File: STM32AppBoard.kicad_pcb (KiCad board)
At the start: 2 copper layers, 85 x 53 mm, 23 parts, among them SW1 SW_Wuerth_450301014042, U1 DM-OLED096-636, U3 NUCLEO-L412KB, U4 JDY-08-jdy-08

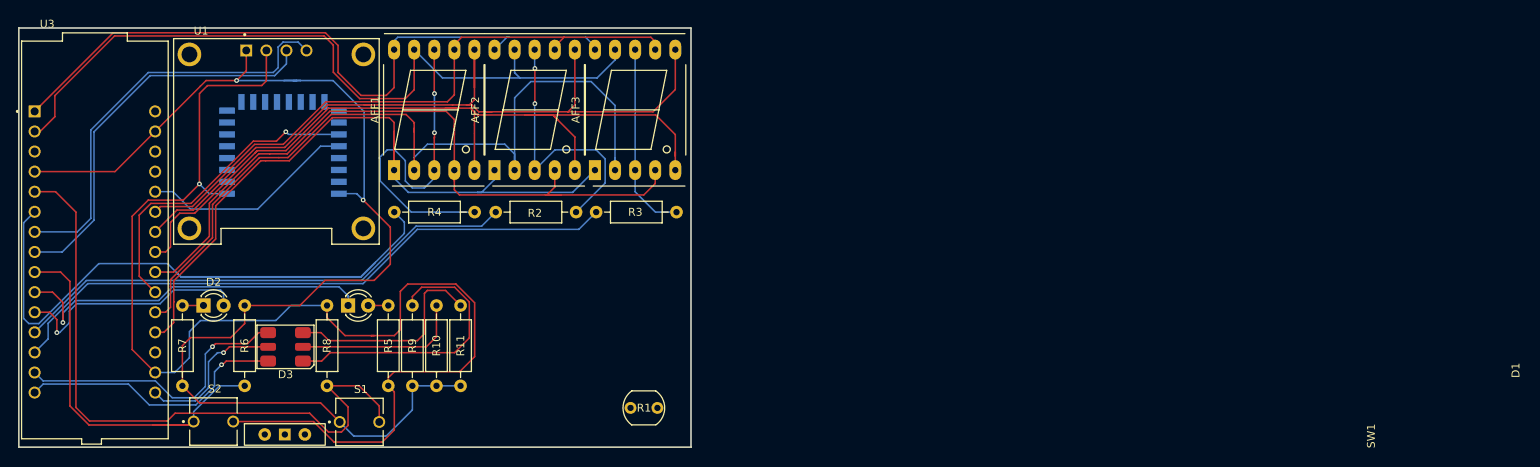
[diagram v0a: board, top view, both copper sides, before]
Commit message: Update STM32AppBoard schematic and PCB layout
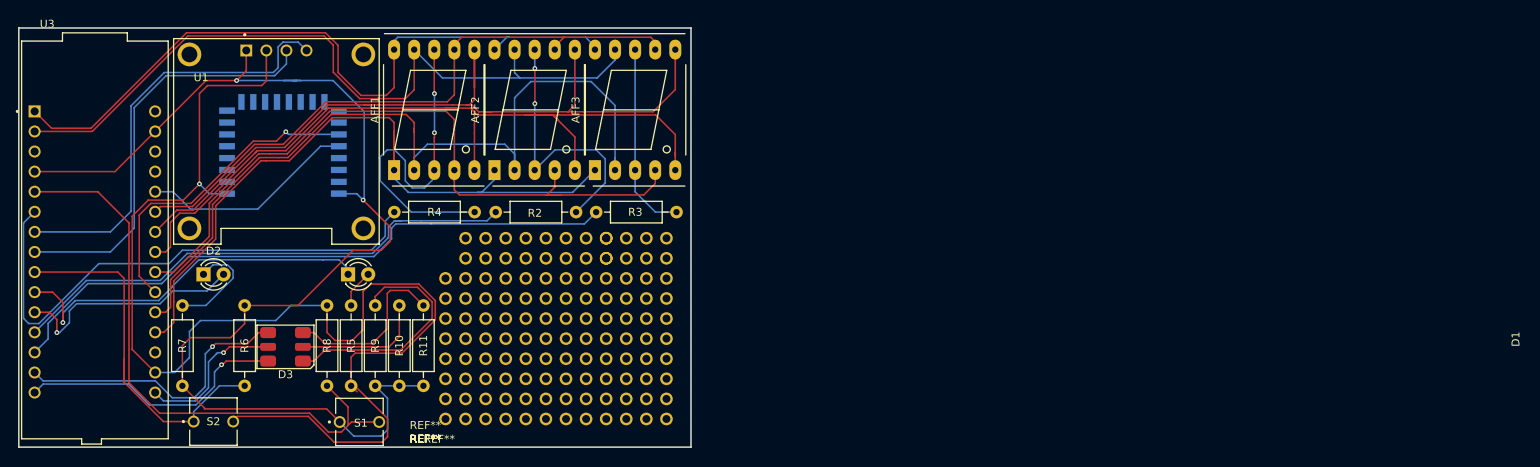
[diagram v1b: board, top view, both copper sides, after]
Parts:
- removed R1: LDR07, OptoDevice:R_LDR_5.1x4.3mm_P3.4mm_Vertical
- removed SW1: SW_Wuerth_450301014042, Button_Switch_THT:SW_Slide-03_Wuerth-WS-SLTV_10x2.5x6.4_P2.54mm
- added REF**: padrray2x4, padarray:padrray2x4, F.Cu at (195.6, 121.9)
- added REF**: padarray, padarray:padarray, F.Cu at (185.4, 134.6)
- added REF**: padrray2x4, padarray:padrray2x4, F.Cu at (188.0, 121.9)
- added REF**: padrray2x4, padarray:padrray2x4, F.Cu at (177.8, 142.2)
- added REF**: padarray, padarray:padarray, F.Cu at (185.4, 124.5)
- added REF**: padrray2x4, padarray:padrray2x4, F.Cu at (177.8, 121.9)
- added REF**: padarray, padarray:padarray, F.Cu at (195.6, 134.6)
- added REF**: padrray2x4, padarray:padrray2x4, F.Cu at (180.3, 134.6)
- added REF**: padrray2x4, padarray:padrray2x4, F.Cu at (177.8, 132.1)
- added REF**: padarray, padarray:padarray, F.Cu at (195.6, 124.5)
- added REF**: padrray2x4, padarray:padrray2x4, F.Cu at (180.3, 124.5)
- moved R10 4.70 mm to (169.4, 127.9)
- moved R11 4.70 mm to (172.5, 127.9)
- moved R5 4.70 mm to (163.3, 138.0)
- moved R9 4.70 mm to (166.4, 127.9)
- moved D1 3.94 mm to (162.9, 124.0)
- moved D2 3.94 mm to (144.7, 124.0)
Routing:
- net /SEL_B: track 97.8 -> 68.2 mm
- net Net-(D2-K): track 2.67 -> 13.4 mm
- net /SW1: track 83.7 -> 74.6 mm
- net Net-(D3-KB): track 36.4 -> 30.3 mm
- net Net-(D3-KG): track 26.8 -> 22.0 mm
- net Net-(D3-KR): track 21.4 -> 16.7 mm
- net /SW2: track 52.3 -> 48.3 mm
- net GND: track 158.4 -> 155.8 mm
- net /SCL: track 49.9 -> 52.3 mm
- net Net-(D1-A): track 2.54 -> 4.83 mm
- net VCC: track 162.6 -> 160.8 mm
- net Net-(AFF1-g): track 90.1 -> 91.9 mm
- net /SEL_A: track 64.6 -> 66.3 mm
- net Net-(AFF1-f): track 98.4 -> 96.8 mm
- net /SDA: track 52.8 -> 54.1 mm
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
